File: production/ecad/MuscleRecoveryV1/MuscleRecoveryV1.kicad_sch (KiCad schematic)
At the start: 18 parts, among them J6 Screw_Terminal_01x06, U4 ESP32-WROOM-32

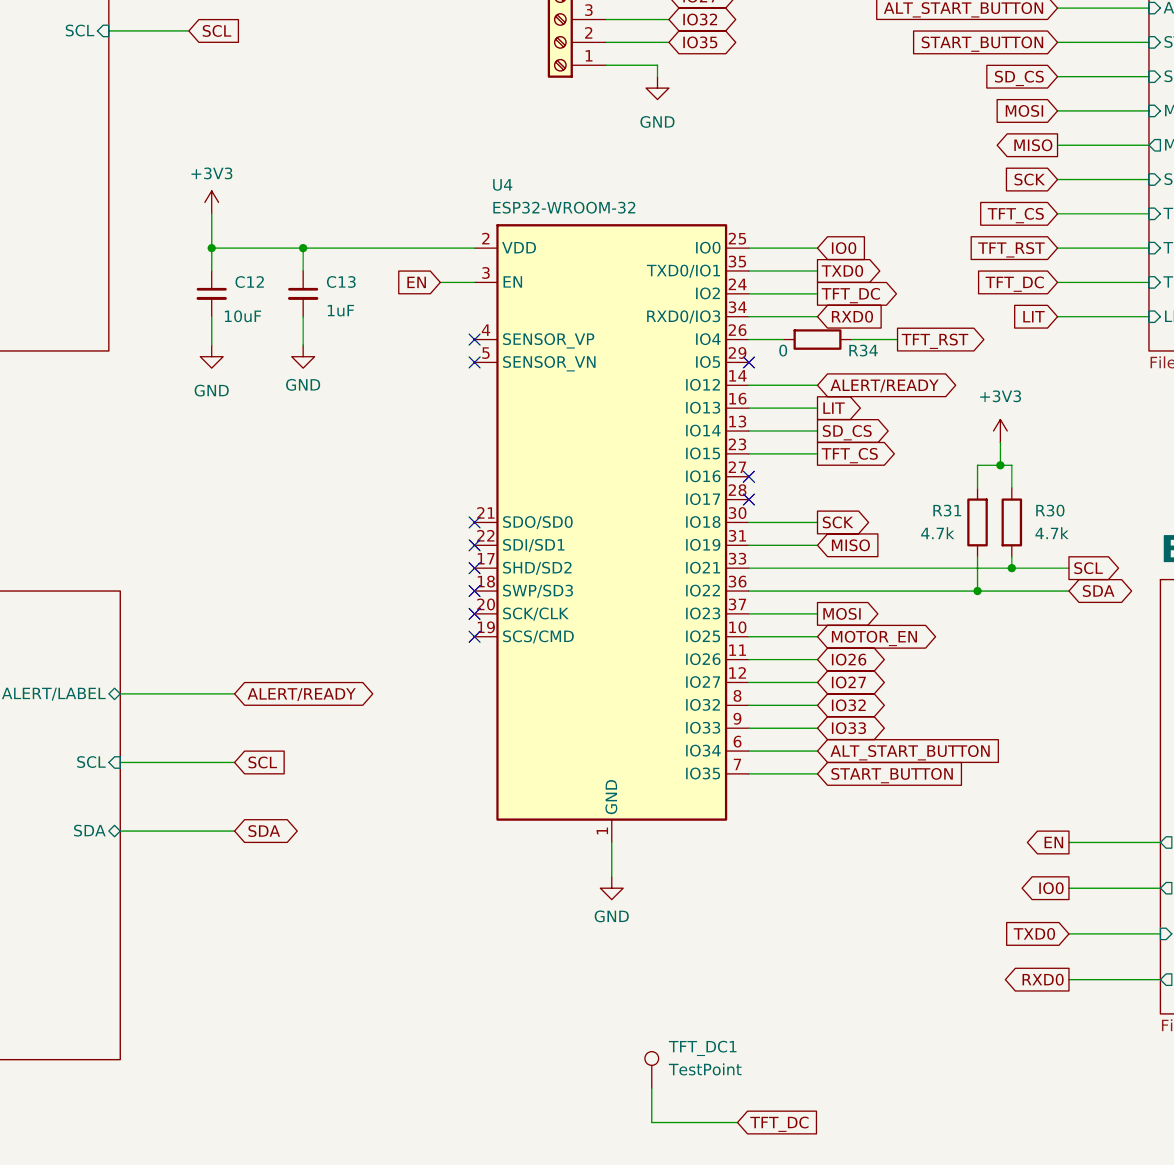
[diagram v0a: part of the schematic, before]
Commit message: added libraries for both the symbols and footprint. Also added updated ESP-32 Symbol and footprint in the library
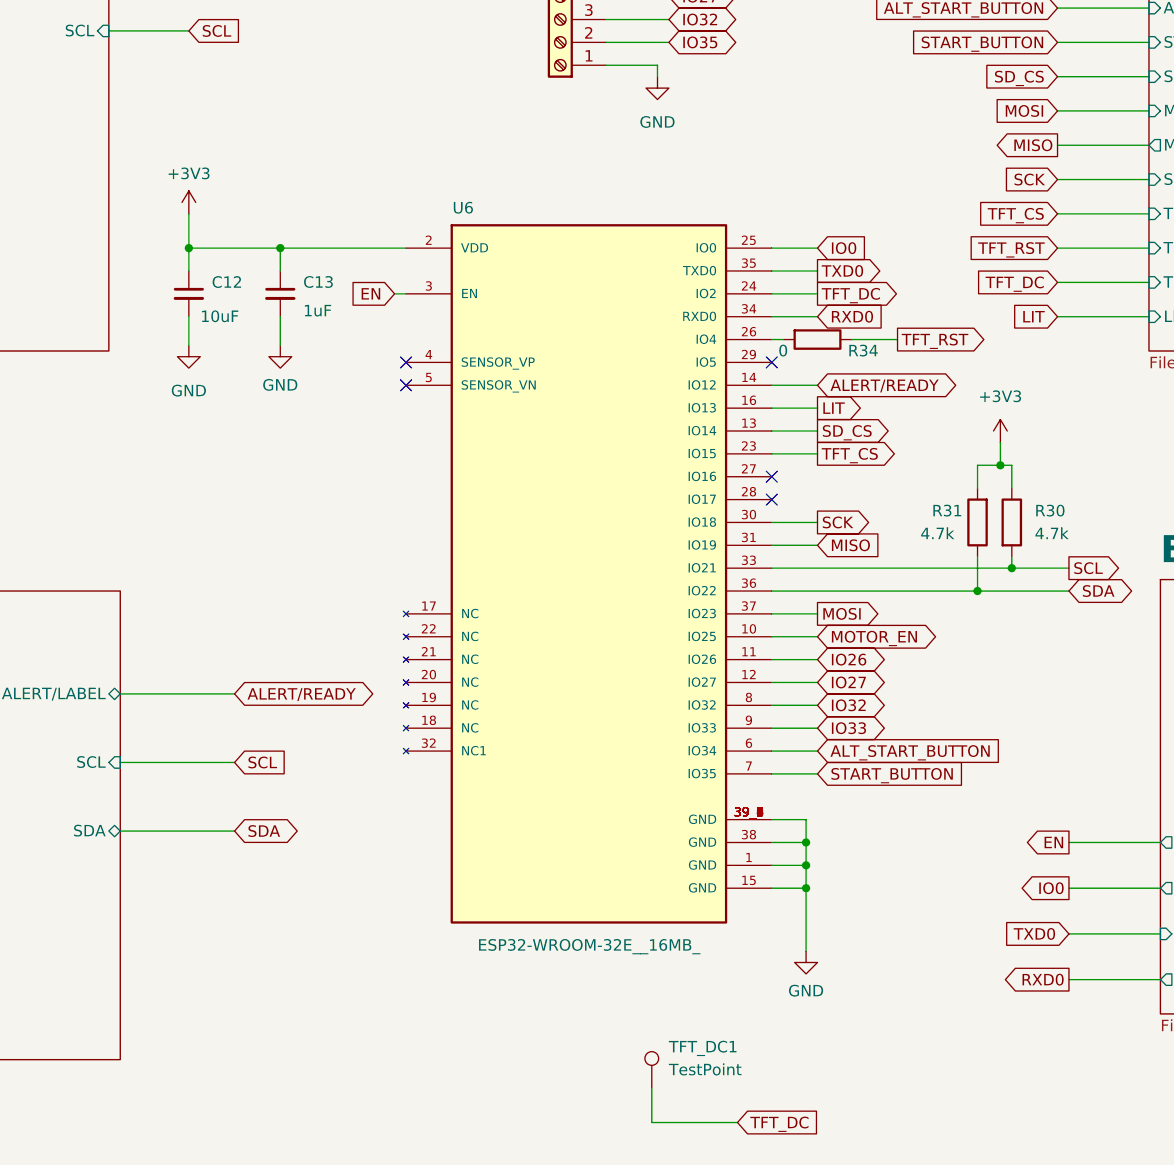
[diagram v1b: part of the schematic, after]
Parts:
- removed U4: ESP32-WROOM-32, RF_Module:ESP32-WROOM-32, symbol RF_Module:ESP32-WROOM-32
- added U6: ESP32-WROOM-32E__16MB_, ESP32-WROOM-32E__16MB_:XCVR_ESP32-WROOM-32E__16MB_, symbol MuscleRecoverySymbolLibray:ESP32-WROOM-32E__16MB_
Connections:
- net +3V3: now also U6.2 (VDD)
- net ALERT/READY: now also U6.14 (IO12)
- net ALT_START_BUTTON: now also U6.6 (IO34)
- net EN: now also U6.3 (EN)
- net GND: now also U6.1 (GND), U6.15 (GND), U6.38 (GND), U6.39_1 (GND), U6.39_2 (GND), U6.39_3 (GND), U6.39_4 (GND), U6.39_5 (GND), U6.39_6 (GND), U6.39_7 (GND), U6.39_8 (GND), U6.39_9 (GND)
- net IO0: now also U6.25 (IO0)
- net IO26: now also U6.11 (IO26)
- net IO27: now also U6.12 (IO27)
- net IO32: now also U6.8 (IO32)
- net IO33: now also U6.9 (IO33)
- net LIT: now also U6.16 (IO13)
- net MISO: now also U6.31 (IO19)
- net MOSI: now also U6.37 (IO23)
- net MOTOR_EN: now also U6.10 (IO25)
- net RXD0: now also U6.34 (RXD0)
- net SCK: now also U6.30 (IO18)
- net SCL: now also U6.33 (IO21)
- net SDA: now also U6.36 (IO22)
- net SD_CS: now also U6.13 (IO14)
- net START_BUTTON: now also U6.7 (IO35)
- net TFT_CS: now also U6.23 (IO15)
- net TFT_DC: now also U6.24 (IO2)
- net TXD0: now also U6.35 (TXD0)
- net at R34.2: now also U6.26 (IO4)
- no-connect marks 11 -> 5
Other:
- moved on the sheet: C12, C13

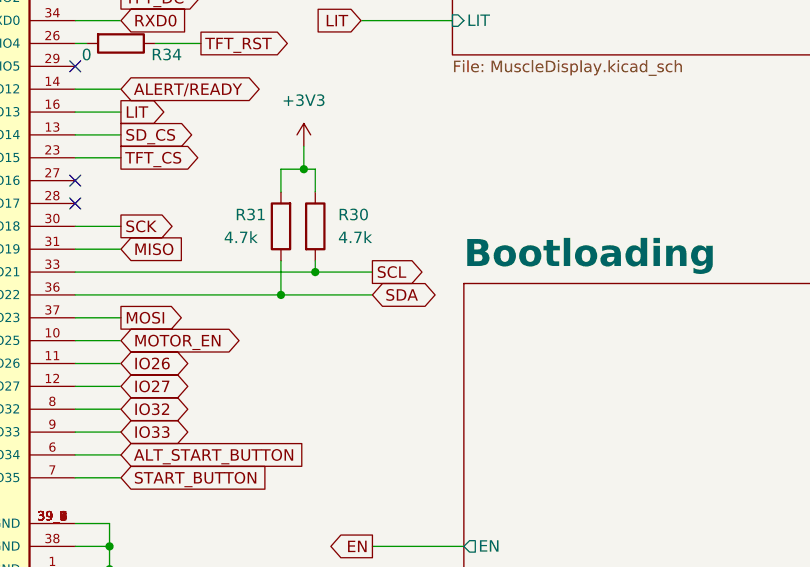
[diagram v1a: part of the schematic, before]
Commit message: updated footprints and emg schematic
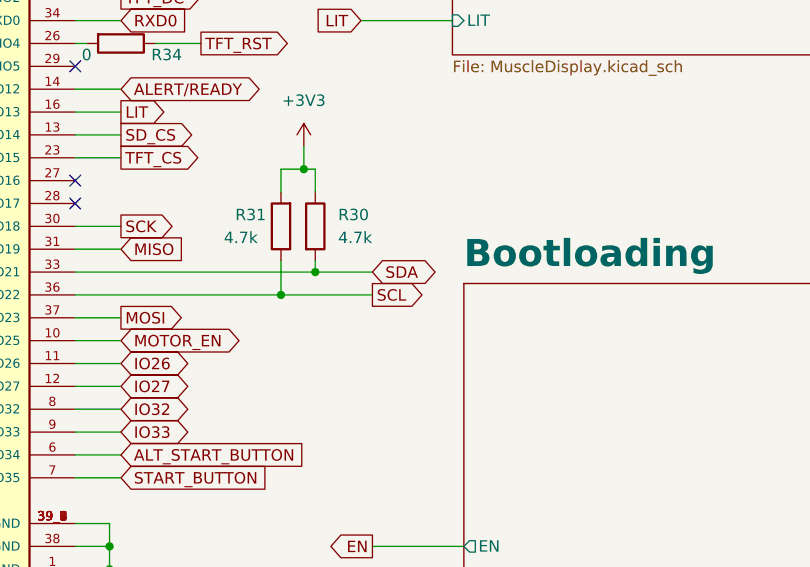
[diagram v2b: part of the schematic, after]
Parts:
- J6: footprint (none) -> Connector_PinHeader_2.54mm:PinHeader_1x06_P2.54mm_Horizontal
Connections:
- net SCL: now also R31.1, U6.36 (IO22); no longer R30.2, U6.33 (IO21)
- net SDA: now also R30.2, U6.33 (IO21); no longer R31.1, U6.36 (IO22)
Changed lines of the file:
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@@
+    )
+  )
+  (global_label "SCL" (shape output) (at 193.04 99.06 0) (fields_autoplaced)
+    (effects (font (size 1.27 1.27)) (justify left))
+    (property "Intersheetrefs" "${INTERSHEET_REFS}" (at 199.5328 99.06 0)
+      (effects (font (size 1.27 1.27)) (justify left) hide)
     )
   )
@@
     )
   )
-  (global_label "SDA" (shape bidirectional) (at 193.04 99.06 0) (fields_autoplaced)
-    (effects (font (size 1.27 1.27)) (justify left))
-    (property "Intersheetrefs" "${INTERSHEET_REFS}" (at 200.7046 99.06 0)
-      (effects (font (size 1.27 1.27)) (justify left) hide)
-    )
-  )
   (global_label "TFT_CLK" (shape input) (at 124.46 173.99 0) (fields_autoplaced)
     (effects (font (size 1.27 1.27)) (justify left))
@@
     )
   )
+  (global_label "SDA" (shape bidirectional) (at 193.04 96.52 0) (fields_autoplaced)
+    (effects (font (size 1.27 1.27)) (justify left))
+    (property "Intersheetrefs" "${INTERSHEET_REFS}" (at 200.7046 96.52 0)
+      (effects (font (size 1.27 1.27)) (justify left) hide)
+    )
+  )
   (global_label "MISO" (shape input) (at 165.1 93.98 0) (fields_autoplaced)
     (effects (font (size 1.27 1.27)) (justify left))
@@
     (property "Intersheetrefs" "${INTERSHEET_REFS}" (at 184.1886 45.72 0)
       (effects (font (size 1.27 1.27)) (justify right) hide)
-    )
-  )
-  (global_label "SCL" (shape output) (at 193.04 96.52 0) (fields_autoplaced)
-    (effects (font (size 1.27 1.27)) (justify left))
-    (property "Intersheetrefs" "${INTERSHEET_REFS}" (at 199.5328 96.52 0)
-      (effects (font (size 1.27 1.27)) (justify left) hide)
     )
   )
@@
       (effects (font (size 1.27 1.27)))
     )
-    (property "Footprint" "" (at 136.525 35.56 0)
-      (effects (font (size 1.27 1.27)) hide)
-    )
+    (property "Footprint" "Connector_PinHeader_2.54mm:PinHeader_1x06_P2.54mm_Horizontal" (at 136.525 35.56 0)
+      (effects (font (size 1.27 1.27)) hide)
+    )

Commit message: updated footprint assignments for ESP32 and S1-S4 to reference the folder Andy made
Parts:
- U6: footprint ESP32-WROOM-32E__16MB_:XCVR_ESP32-WROOM-32E__16MB_ -> Muscle_Recovery_Footprint_Library:XCVR_ESP32-WROOM-32E__16MB_
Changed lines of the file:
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@@
       (effects (font (size 1.27 1.27)))
     )
-    (property "Footprint" "ESP32-WROOM-32E__16MB_:XCVR_ESP32-WROOM-32E__16MB_" (at 143.51 144.78 0)
+    (property "Footprint" "Muscle_Recovery_Footprint_Library:XCVR_ESP32-WROOM-32E__16MB_" (at 143.51 144.78 0)
       (effects (font (size 1.27 1.27)) (justify bottom) hide)
     )

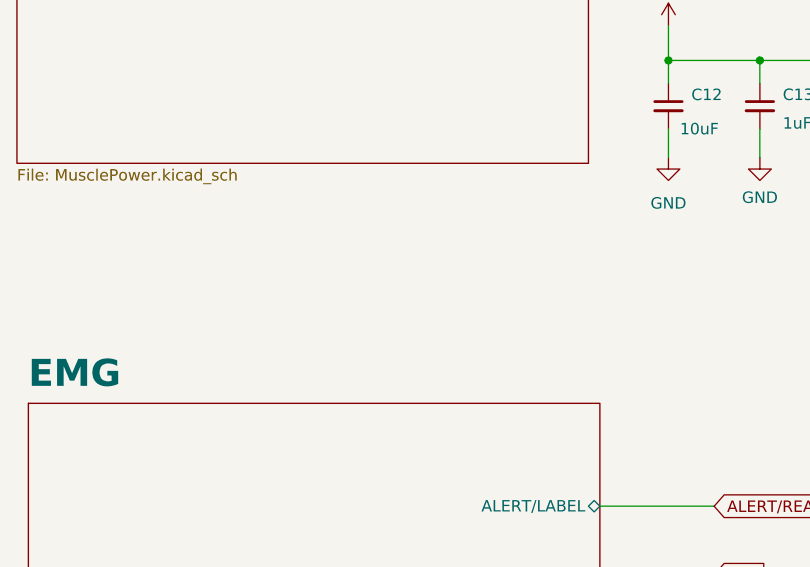
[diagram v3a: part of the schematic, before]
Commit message: supposedly finished schematic and footprints and started PCB
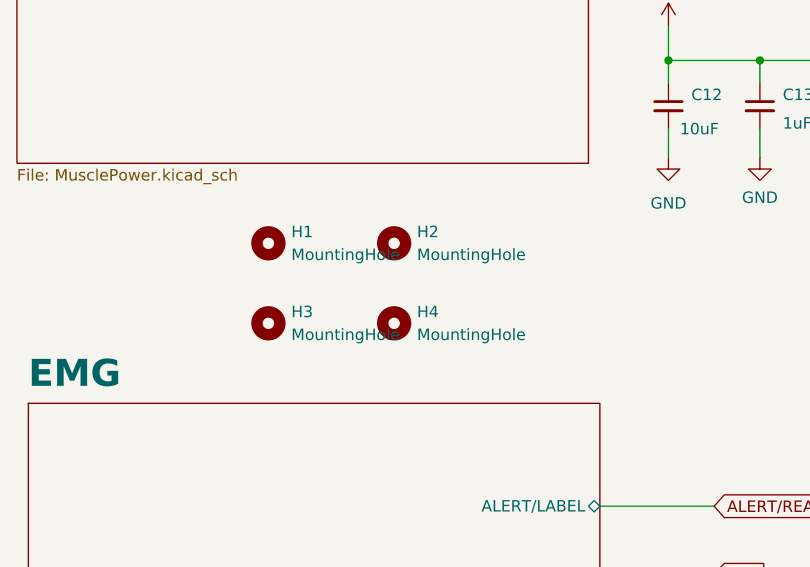
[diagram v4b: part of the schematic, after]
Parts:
- added H1, H2, H3, H4: MountingHole, MountingHole:MountingHole_2.2mm_M2, symbol Mechanical:MountingHole
- J6: footprint Connector_PinHeader_2.54mm:PinHeader_1x06_P2.54mm_Horizontal -> Connector_PinHeader_2.54mm:PinHeader_1x06_P2.54mm_Vertical
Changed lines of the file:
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@@
+    )
+  )
+  (symbol (lib_id "Mechanical:MountingHole") (at 50.8 90.17 0) (unit 1)
+    (in_bom yes) (on_board yes) (dnp no) (fields_autoplaced)
+    (property "Reference" "H3" (at 53.34 88.9 0)
+      (effects (font (size 1.27 1.27)) (justify left))
+    )
+    (property "Value" "MountingHole" (at 53.34 91.44 0)
+      (effects (font (size 1.27 1.27)) (justify left))
+    )
+    (property "Footprint" "MountingHole:MountingHole_2.2mm_M2" (at 50.8 90.17 0)
+      (effects (font (size 1.27 1.27)) hide)
+    )
+    (property "Datasheet" "~" (at 50.8 90.17 0)
+      (effects (font (size 1.27 1.27)) hide)
+    )
+    (instances
+      (project "MuscleRecoveryV1"
+        (path "/4e550305-79d2-4e4a-a502-817ebcc79f9a"
+          (reference "H3") (unit 1)
+        )
+      )
     )
   )
@@
       (effects (font (size 1.27 1.27)))
     )
-    (property "Footprint" "Connector_PinHeader_2.54mm:PinHeader_1x06_P2.54mm_Horizontal" (at 136.525 35.56 0)
+    (property "Footprint" "Connector_PinHeader_2.54mm:PinHeader_1x06_P2.54mm_Vertical" (at 136.525 35.56 0)
       (effects (font (size 1.27 1.27)) hide)
     )
@@
     )
   )
+  (symbol (lib_id "Mechanical:MountingHole") (at 64.77 90.17 0) (unit 1)
+    (in_bom yes) (on_board yes) (dnp no) (fields_autoplaced)
+    (property "Reference" "H4" (at 67.31 88.9 0)
+      (effects (font (size 1.27 1.27)) (justify left))
+    )
+    (property "Value" "MountingHole" (at 67.31 91.44 0)
+      (effects (font (size 1.27 1.27)) (justify left))
+    )
+    (property "Footprint" "MountingHole:MountingHole_2.2mm_M2" (at 64.77 90.17 0)
+      (effects (font (size 1.27 1.27)) hide)
+    )
+    (property "Datasheet" "~" (at 64.77 90.17 0)
+      (effects (font (size 1.27 1.27)) hide)
+    )
+    (instances
+      (project "MuscleRecoveryV1"
+        (path "/4e550305-79d2-4e4a-a502-817ebcc79f9a"
+          (reference "H4") (unit 1)
+        )
+      )
+    )
+  )
   (symbol (lib_id "Connector:TestPoint") (at 86.995 169.545 0) (unit 1)
     (in_bom yes) (on_board yes) (dnp no) (fields_autoplaced)
@@
         )
       )
+    )
+  )
+  (symbol (lib_id "Mechanical:MountingHole") (at 64.77 81.28 0) (unit 1)
+    (in_bom yes) (on_board yes) (dnp no) (fields_autoplaced)
+    (property "Reference" "H2" (at 67.31 80.01 0)
+      (effects (font (size 1.27 1.27)) (justify left))
+    )
+    (property "Value" "MountingHole" (at 67.31 82.55 0)
+      (effects (font (size 1.27 1.27)) (justify left))
+    )
+    (property "Footprint" "MountingHole:MountingHole_2.2mm_M2" (at 64.77 81.28 0)
+      (effects (font (size 1.27 1.27)) hide)
+    )
+    (property "Datasheet" "~" (at 64.77 81.28 0)
+      (effects (font (size 1.27 1.27)) hide)
+    )
+    (instances
+      (project "MuscleRecoveryV1"
+        (path "/4e550305-79d2-4e4a-a502-817ebcc79f9a"
+          (reference "H2") (unit 1)
+        )
+      )
+    )
+  )
+  (symbol (lib_id "Mechanical:MountingHole") (at 50.8 81.28 0) (unit 1)
+    (in_bom yes) (on_board yes) (dnp no) (fields_autoplaced)
+    (property "Reference" "H1" (at 53.34 80.01 0)
+      (effects (font (size 1.27 1.27)) (justify left))
+    )
+    (property "Value" "MountingHole" (at 53.34 82.55 0)
+      (effects (font (size 1.27 1.27)) (justify left))
+    )
+    (property "Footprint" "MountingHole:MountingHole_2.2mm_M2" (at 50.8 81.28 0)
+      (effects (font (size 1.27 1.27)) hide)
+    )
+    (property "Datasheet" "~" (at 50.8 81.28 0)
+      (effects (font (size 1.27 1.27)) hide)
+    )
+    (instances
+      (project "MuscleRecoveryV1"
+        (path "/4e550305-79d2-4e4a-a502-817ebcc79f9a"
+          (reference "H1") (unit 1)
+        )
+      )

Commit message: pushing current layout and other changes to be able to pull
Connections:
- net IO35 is gone; now on net IO17: J6.2 (Pin_2)
- net TFT_CLK is gone; now on net SCK: TFT_CLK1.1
- net SCL: now also SCL1.1
- net SDA: no longer SCL1.1
- net IO17: now reaches U6.28 (IO17)
- no-connect marks 5 -> 4
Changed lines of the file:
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@@
   (no_connect (at 160.02 86.36))
   (no_connect (at 160.02 73.66))
-  (no_connect (at 160.02 88.9))
   (no_connect (at 119.38 76.2))
   (no_connect (at 119.38 73.66))
@@
   )
   (wire (pts (xy 191.77 68.58) (xy 201.93 68.58))
+    (stroke (width 0) (type default))
+  )
+  (wire (pts (xy 160.02 88.9) (xy 165.1 88.9))
     (stroke (width 0) (type default))
   )
@@
     )
   )
-  (global_label "SDA" (shape input) (at 65.405 189.865 0) (fields_autoplaced)
-    (effects (font (size 1.27 1.27)) (justify left))
-    (property "Intersheetrefs" "${INTERSHEET_REFS}" (at 71.9583 189.865 0)
+  (global_label "SCL" (shape input) (at 65.405 189.865 0) (fields_autoplaced)
+    (effects (font (size 1.27 1.27)) (justify left))
+    (property "Intersheetrefs" "${INTERSHEET_REFS}" (at 71.8978 189.865 0)
       (effects (font (size 1.27 1.27)) (justify left) hide)
     )
@@
     )
   )
-  (global_label "TFT_CLK" (shape input) (at 124.46 173.99 0) (fields_autoplaced)
-    (effects (font (size 1.27 1.27)) (justify left))
-    (property "Intersheetrefs" "${INTERSHEET_REFS}" (at 135.0047 173.99 0)
-      (effects (font (size 1.27 1.27)) (justify left) hide)
-    )
-  )
   (global_label "MOSI" (shape output) (at 165.1 101.6 0) (fields_autoplaced)
     (effects (font (size 1.27 1.27)) (justify left))
@@
     )
   )
-  (global_label "IO35" (shape bidirectional) (at 148.59 38.1 0) (fields_autoplaced)
+  (global_label "IO17" (shape bidirectional) (at 165.1 88.9 0) (fields_autoplaced)
+    (effects (font (size 1.27 1.27)) (justify left))
+    (property "Intersheetrefs" "${INTERSHEET_REFS}" (at 173.5508 88.9 0)
+      (effects (font (size 1.27 1.27)) (justify left) hide)
+    )
+  )
+  (global_label "IO17" (shape bidirectional) (at 148.59 38.1 0) (fields_autoplaced)
     (effects (font (size 1.27 1.27)) (justify left))
     (property "Intersheetrefs" "${INTERSHEET_REFS}" (at 157.0408 38.1 0)
@@
     (property "Intersheetrefs" "${INTERSHEET_REFS}" (at 182.3139 57.15 0)
       (effects (font (size 1.27 1.27)) (justify right) hide)
+    )
+  )
+  (global_label "SCK" (shape input) (at 124.46 173.99 0) (fields_autoplaced)
+    (effects (font (size 1.27 1.27)) (justify left))
+    (property "Intersheetrefs" "${INTERSHEET_REFS}" (at 131.1947 173.99 0)
+      (effects (font (size 1.27 1.27)) (justify left) hide)
     )
   )
@@
   )
   (symbol (lib_id "Connector:TestPoint") (at 55.88 170.18 0) (unit 1)
-    (in_bom yes) (on_board yes) (dnp no) (fields_autoplaced)
+    (in_bom yes) (on_board yes) (dnp no)
     (property "Reference" "SDA1" (at 57.785 165.608 0)
       (effects (font (size 1.27 1.27)) (justify left))
     )
     (property "Value" "TestPoint" (at 57.785 168.148 0)
-      (effects (font (size 1.27 1.27)) (justify left))
+      (effects (font (size 1.27 1.27)) (justify right))
     )
     (property "Footprint" "TestPoint:TestPoint_Pad_D1.5mm" (at 60.96 170.18 0)
@@
       (effects (font (size 1.27 1.27)) (justify left top))
     )
-    (pin "SDA" bidirectional (at 86.36 30.48 0)
-      (effects (font (size 1.27 1.27)) (justify right))
-    )
-    (pin "SCL" input (at 86.36 36.83 0)
-      (effects (font (size 1.27 1.27)) (justify right))
-    )
-    (instances
+    (pin "SDA" bidirectional (at 22.86 30.48 180)
+      (effects (font (size 1.27 1.27)) (justify left))
+    )
+    (pin "SCL" input (at 22.86 36.83 180)
+      (effects (font (size 1.27 1.27)) (justify left))
+    )
+    (instances

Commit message: saving changes
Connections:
- net IO17: now also J6.3 (Pin_3); no longer J6.2 (Pin_2)
- net IO26: now also J6.4 (Pin_4); no longer J6.5 (Pin_5)
- net IO27: now also J6.5 (Pin_5); no longer J6.4 (Pin_4)
- net IO32: now also J6.2 (Pin_2); no longer J6.3 (Pin_3)
